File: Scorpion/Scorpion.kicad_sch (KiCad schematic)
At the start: 249 parts, among them SW1 TURBO

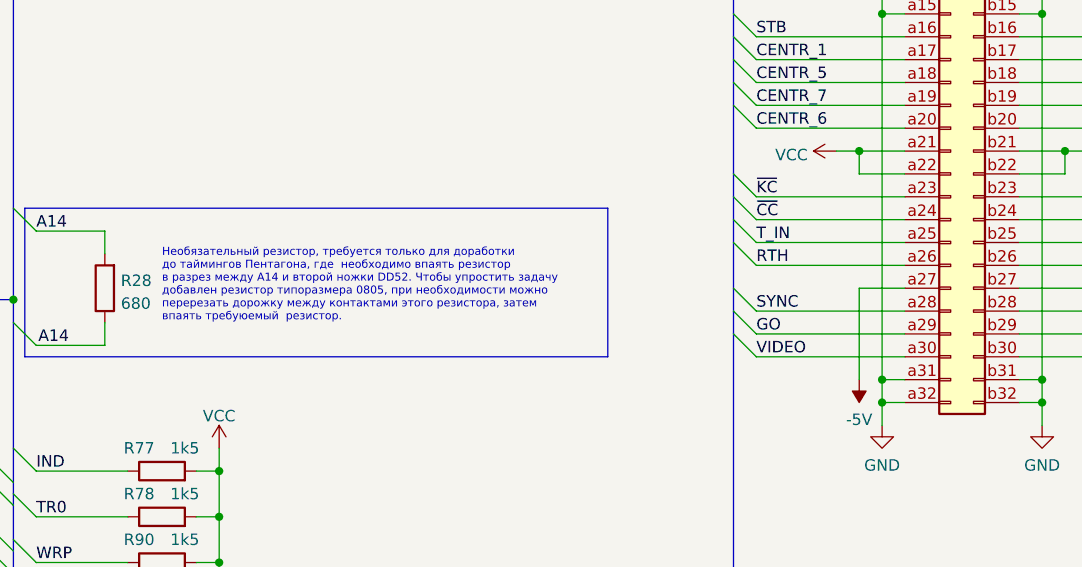
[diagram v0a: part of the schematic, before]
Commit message: Port 7FFD decryption fix described.
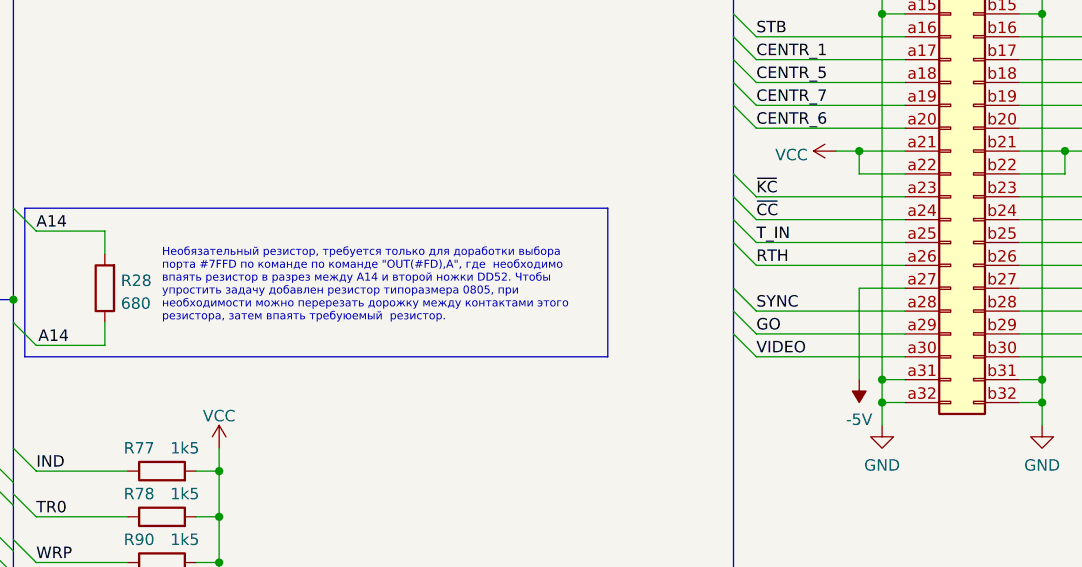
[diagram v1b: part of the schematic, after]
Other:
- note added: "Необязательный резистор, требуется только для доработки выбора порта #7FFD по команде по команде "OUT(#FD),A", где необходимо впаять резистор в разрез между A14 и второй ножки DD52. Чтобы упростить задачу добавлен резистор типоразмера 0805, при необходимости можно перерезать дорожку между контактами этого резистора, затем впаять требуюемый резистор."
- note removed: "Необязательный резистор, требуется только для доработки до таймингов Пентагона, где необходимо впаять резистор в разрез между A14 и второй ножки DD52. Чтобы упростить задачу добавлен резистор типоразмера 0805, при необходимости можно перерезать дорожку между контактами этого резистора, затем впаять требуюемый резистор."
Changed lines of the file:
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@@
     (effects (font (size 1.27 1.27)) (justify left bottom))
   )
-  (text "Необязательный резистор, требуется только для доработки\nдо таймингов Пентагона, где  необходимо впаять резистор \nв разрез между A14 и второй ножки DD52. Чтобы упростить задачу \nдобавлен резистор типоразмера 0805, при необходимости можно\nперерезать дорожку между контактами этого резистора, затем\nвпаять требуюемый  резистор."
+  (text "Необязательный резистор, требуется только для доработки выбора \nпорта #7FFD по команде по команде \"OUT(#FD),A\", где  необходимо \nвпаять резистор в разрез между A14 и второй ножки DD52. Чтобы \nупростить задачу добавлен резистор типоразмера 0805, при \nнеобходимости можно перерезать дорожку между контактами этого \nрезистора, затем впаять требуюемый  резистор."
     (at 491.49 359.41 0)
     (effects (font (size 0.889 0.889)) (justify left bottom))

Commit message: Fixed minor silkscreen typos Sync Alternative and Value fields Remove unused user layers
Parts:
- C10: value 100uF -> 100u
- C16, C17: value 150 -> 150p
- C9: value 33uF -> 33u
- DD10: Alt 74LS02 -> 74ALS02
- DD12, DD48, DD69: Alt 74LS00 -> 74ALS00
- DD13, DD66: Alt 74LS08 -> 74ALS08
- DD30, DD41: Alt (none) -> GAL22V10
- DD32, DD52, DD65: Alt 74LS138 -> 74ALS138
- DD33, DD34: Alt 74LS298 -> 74ALS298
- DD35, DD46, DD47, DD54, DD57: Alt 74LS174 -> 74ALS174
- DD38: Alt 74LS373 -> 74ALS373
- DD39: Alt 74LS166 -> 74ALS166
- DD40, DD62: Alt 74LS295 -> 74ALS295
- DD42, DD50, DD55, DD56: Alt 74LS74 -> 74ALS74
- DD45: Alt 74LS253 -> 74ALS253
- DD49: Alt 74LS30 -> 74ALS30
- DD53, DD58: Alt 74LS374 -> 74ALS374
- DD59: Alt (none) -> GAL16V8B
- DD60: Alt (none) -> MB8877A
- DD63: Alt 74LS38 -> 74ALS38
- DD67: Alt 74LS27 -> 74ALS27
- DD68: Alt 74LS04 -> 74ALS04
- DD70: symbol Scorpion:К561ЛН2 -> 4xxx:4069; Alt 74LS05 -> CD4069
- SW1: Alt (none) -> 2 pin 2.54mm
- VD1, VD10, VD11, VD12, VD13, VD16, VD17, VD2, VD3, VD4, VD5, VD6, VD7, VD9: value 1N4148 -> КД522А; Alt (none) -> 1N4148
- VD8: footprint LED_THT:LED_D3.0mm -> Scorpion:LED_D3.0mm; Alt (none) -> LED 3mm, Header 2.54mm 2 pin
- XP6: footprint Scorpion:CONN_2x32_EDGE -> Scorpion:CONN_2x32_EDGE_2.52
- XP7: footprint Scorpion:CONN_2x30_EDGE -> Scorpion:CONN_2x30_EDGE_2.52
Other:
- note added: "Краевой разъем шины"
- note added: "Разъем шины DIP 2 ряда ножек"
- note added: "Разъем шины DIP 3 ряда ножек"
- note added: "Системный краевой разъем"
- note added: "Системный разъем DIP"

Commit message: Fix R/Ro and G/Go signals
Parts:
- added C44, C45, C46: 0.1u, Scorpion:Cap_5.08, symbol Device:C
- DD35, DD46, DD47, DD54, DD57: value K1533TM9 -> К1533ТМ9
- H1, H2, H3, H4: value MountingHole -> ~
- R28: now not fitted
- XP11: footprint Scorpion:CONN_2x17_EDGE -> Scorpion:CONN_2x17_EDGE_NARROW
- ZQ1: footprint Crystal:Crystal_HC50_Horizontal_1EP_style2 -> Crystal:Crystal_HC49-U_Horizontal_1EP_style2
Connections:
- net G: now also DD43.4 (Za), R15.2; no longer DD43.7 (Zb), R16.2
- net GND: now also C44.1, C45.1, C46.1
- net GO: now also R2.1; no longer R4.1
- net R: now also DD43.7 (Zb), R16.2; no longer DD43.4 (Za), R15.2
- net RO: now also R4.1; no longer R2.1
- net VCC: now also C44.2, C45.2, C46.2
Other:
- moved on the sheet: C11, C13, C14, C15, C16, C20, C22, C23, C24, C25, C26, C27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
